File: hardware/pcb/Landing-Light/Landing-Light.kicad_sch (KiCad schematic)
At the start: 51 parts, among them J1 Conn_01x04, J3 USB_C_Receptacle_USB2.0_16P, Q2 NMOS, Q3 NMOS, Q4 PMOS, SW1 SW_SPDT, SW2 SW_SP3T, U1 BQ25172DSGR, U2 SRV05-4, U3 TPS61200DRC

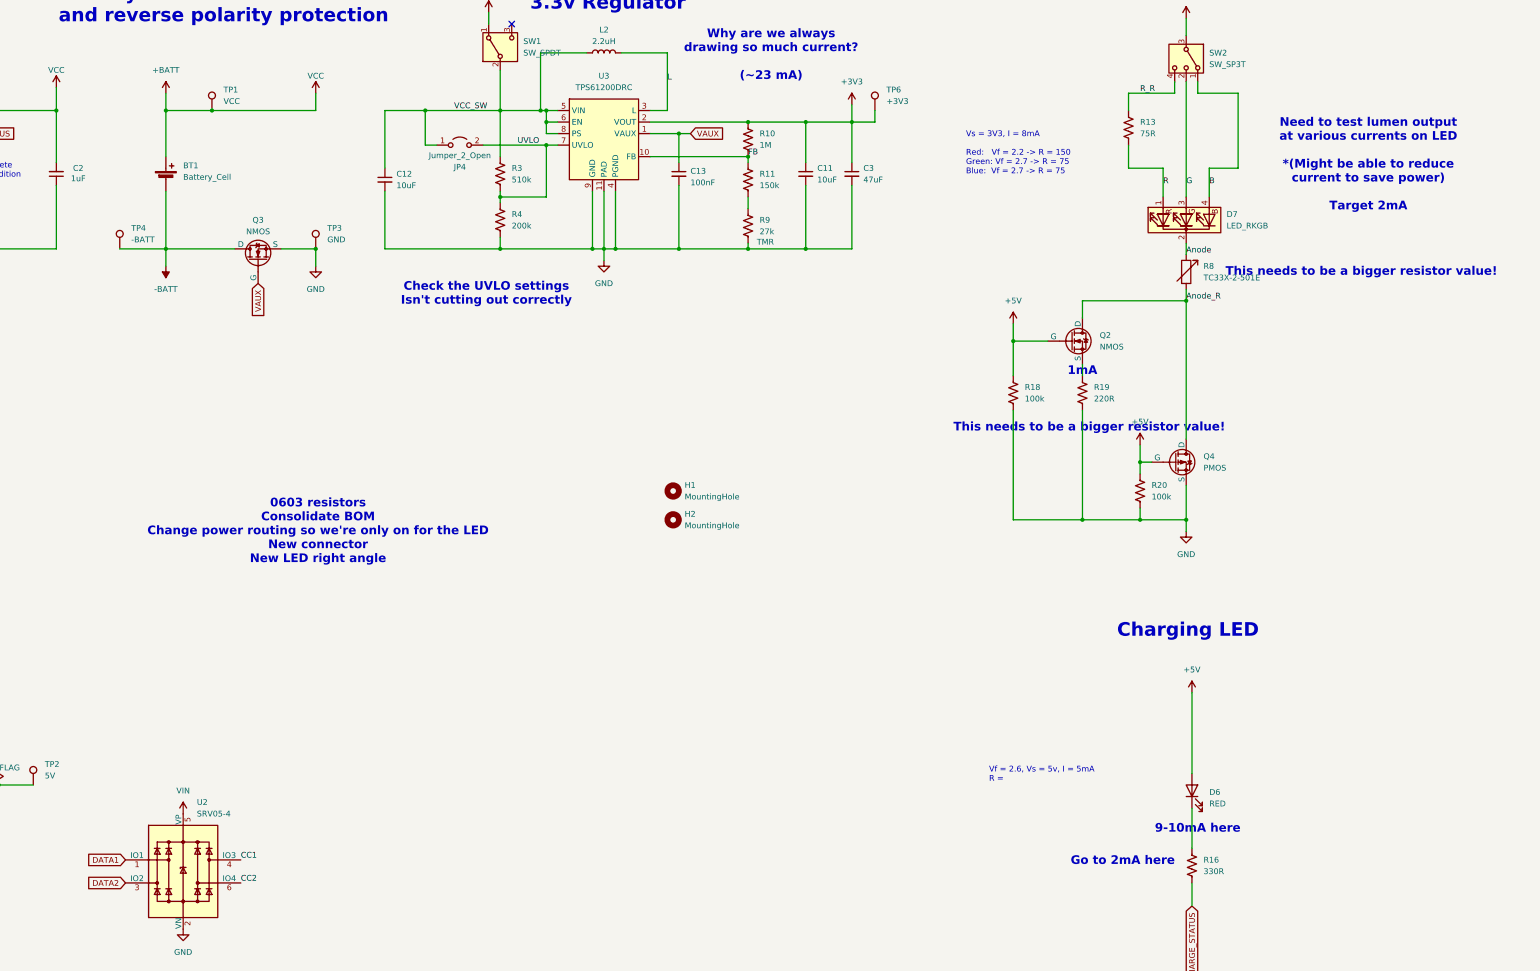
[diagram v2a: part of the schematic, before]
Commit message: Clean ground plane
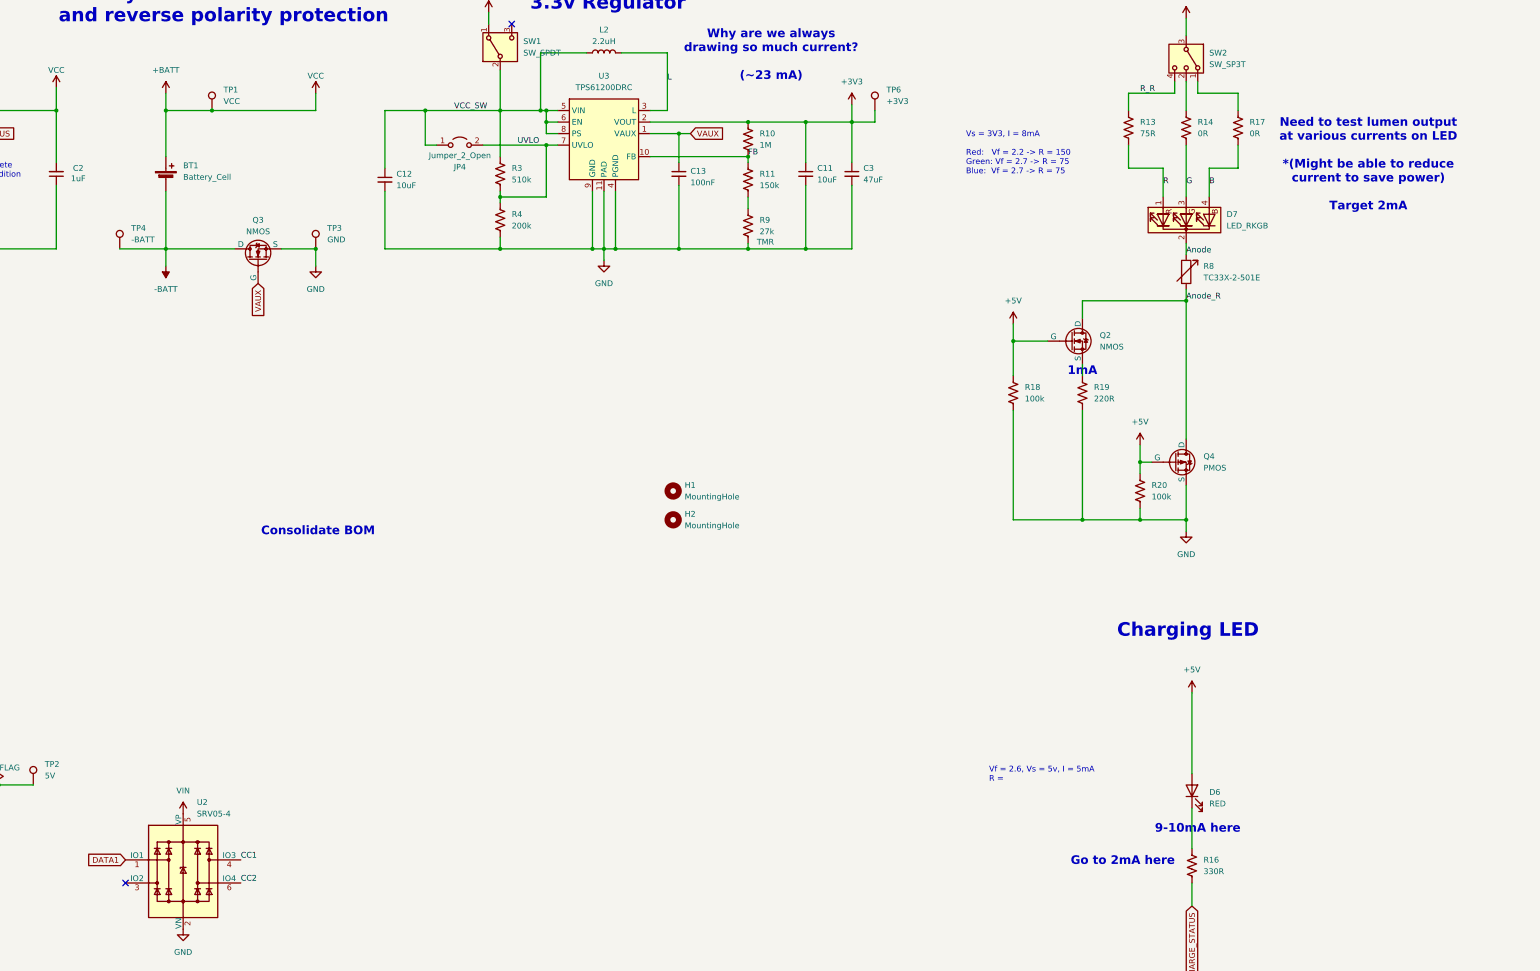
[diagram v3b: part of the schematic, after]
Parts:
- added R14, R17: 0R, Resistor_SMD:R_0402_1005Metric, symbol Device:R_US
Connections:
- net B: now also R17.2; no longer SW2.1
- net DATA2: no longer U2.3 (IO2)
- net G: now also R14.2; no longer SW2.2
- new net: R17.1, SW2.1
- new net: R14.1, SW2.2
- no-connect marks 7 -> 8
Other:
- note added: "Consolidate BOM"
- note removed: "0603 resistors Consolidate BOM Change power routing so we're only on for the LED New connector New LED right angle"
- note removed: "Check the UVLO settings Isn't cutting out correctly"
- note removed: "This needs to be a bigger resistor value!"
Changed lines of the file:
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@@
 	(generator_version "9.0")
 	(paper "A3")
-	(text "This needs to be a bigger resistor value!"
-		(exclude_from_sim no)
-		(at 418.338 88.9 0)
-		(effects
-			(font
-				(size 1.905 1.905)
-				(thickness 0.381)
-				(bold yes)
-				(color 255 0 0 1)
-			)
-		)
-	)
 	(text "Battery \nand reverse polarity protection"
 		(exclude_from_sim no)
@@
 		)
 	)
-	(text "This needs to be a bigger resistor value!"
-		(exclude_from_sim no)
-		(at 358.394 123.19 0)
-		(effects
-			(font
-				(size 1.905 1.905)
-				(thickness 0.381)
-				(bold yes)
-				(color 255 0 0 1)
-			)
-		)
-	)
-	(text "0603 resistors\nConsolidate BOM\nChange power routing so we're only on for the LED\nNew connector\nNew LED right angle"
+	(text "Consolidate BOM"
 		(exclude_from_sim no)
 		(at 188.468 146.05 0)
@@
 		)
 	)
-	(text "Check the UVLO settings\nIsn't cutting out correctly"
-		(exclude_from_sim no)
-		(at 225.552 93.726 0)
-		(effects
-			(font
-				(size 1.905 1.905)
-				(thickness 0.381)
-				(bold yes)
-				(color 255 0 0 1)
-			)
-		)
-	)
 	(text "USB-C Connector"
 		(exclude_from_sim no)
@@
 		(at 66.04 217.17)
 	)
+	(no_connect
+		(at 146.05 223.52)
+	)
 	(wire
 		(pts
@@
 	(wire
 		(pts
+			(xy 391.16 60.96) (xy 391.16 66.04)
+		)
+		(stroke
+			(width 0)
+			(type default)
+		)
+	)
+	(wire
+		(pts
 			(xy 356.87 109.22) (xy 356.87 111.76)
 		)
@@
 	(wire
 		(pts
+			(xy 391.16 49.53) (xy 391.16 53.34)
+		)
+		(stroke
+			(width 0)
+			(type default)
+		)
+	)
+	(wire
+		(pts
 			(xy 261.62 63.5) (xy 283.21 63.5)
 		)
@@
 	(wire
 		(pts
+			(xy 379.73 60.96) (xy 379.73 72.39)
+		)
+		(stroke
+			(width 0)
+			(type default)
+		)
+	)
+	(wire
+		(pts
 			(xy 379.73 143.51) (xy 379.73 146.05)
 		)
@@
 	(wire
 		(pts
-			(xy 379.73 46.99) (xy 379.73 72.39)
+			(xy 71.12 83.82) (xy 88.9 83.82)
 		)
 		(stroke
@@
 	(wire
 		(pts
-			(xy 71.12 83.82) (xy 88.9 83.82)
+			(xy 295.91 64.77) (xy 295.91 55.88)
 		)
 		(stroke
@@
 	(wire
 		(pts
-			(xy 295.91 64.77) (xy 295.91 55.88)
+			(xy 73.66 209.55) (xy 66.04 209.55)
 		)
 		(stroke
@@
 	(wire
 		(pts
-			(xy 73.66 209.55) (xy 66.04 209.55)
+			(xy 72.39 181.61) (xy 72.39 179.07)
 		)
 		(stroke
@@
 	(wire
 		(pts
-			(xy 72.39 181.61) (xy 72.39 179.07)
+			(xy 228.6 63.5) (xy 228.6 53.34)
 		)
 		(stroke
@@
 	(wire
 		(pts
-			(xy 228.6 63.5) (xy 228.6 53.34)
+			(xy 379.73 46.99) (xy 379.73 53.34)
 		)
 		(stroke
@@
 	(wire
 		(pts
-			(xy 391.16 49.53) (xy 391.16 66.04)
-		)
-		(stroke
-			(width 0)
-			(type default)
-		)
-	)
-	(wire
-		(pts
 			(xy 226.06 31.75) (xy 226.06 34.29)
 		)
@@
 		)
 	)
-	(global_label "DATA2"
-		(shape input)
-		(at 146.05 223.52 180)
-		(fields_autoplaced yes)
-		(effects
-			(font
-				(size 1.27 1.27)
-			)
-			(justify right)
-		)
-		(property "Intersheetrefs" "${INTERSHEET_REFS}"
-			(at 137.4405 223.52 0)
-			(effects
-				(font
-					(size 1.27 1.27)
-				)
-				(justify right)
-				(hide yes)
-			)
-		)
-	)
 	(global_label "DATA1"
 		(shape input)
-		(at 146.05 218.44 180)
+		(at 72.39 173.99 90)
 		(fields_autoplaced yes)
 		(effects
@@
 				(size 1.27 1.27)
 			)
-			(justify right)
+			(justify left)
 		)
 		(property "Intersheetrefs" "${INTERSHEET_REFS}"
-			(at 137.4405 218.44 0)
+			(at 72.39 165.3805 90)
 			(effects
 				(font
 					(size 1.27 1.27)
 				)
-				(justify right)
+				(justify left)
 				(hide yes)
 			)
 		)
 	)
-	(global_label "DATA1"
+	(global_label "VAUX"
 		(shape input)
-		(at 72.39 173.99 90)
+		(at 270.51 58.42 0)
 		(fields_autoplaced yes)
 		(effects
@@
 		)
 		(property "Intersheetrefs" "${INTERSHEET_REFS}"
-			(at 72.39 165.3805 90)
+			(at 278.2124 58.42 0)
 			(effects
 				(font
@@
 	(global_label "VAUX"
 		(shape input)
-		(at 270.51 58.42 0)
+		(at 175.26 91.44 270)
 		(fields_autoplaced yes)
 		(effects
@@
 				(size 1.27 1.27)
 			)
-			(justify left)
+			(justify right)
 		)
 		(property "Intersheetrefs" "${INTERSHEET_REFS}"
-			(at 278.2124 58.42 0)
+			(at 175.26 99.1424 90)
 			(effects
 				(font
 					(size 1.27 1.27)
 				)
-				(justify left)
+				(justify right)
 				(hide yes)
 			)
 		)
 	)
-	(global_label "VAUX"
+	(global_label "DATA1"
 		(shape input)
-		(at 175.26 91.44 270)
+		(at 146.05 218.44 180)
 		(fields_autoplaced yes)
 		(effects
@@
 		)
 		(property "Intersheetrefs" "${INTERSHEET_REFS}"
-			(at 175.26 99.1424 90)
+			(at 137.4405 218.44 0)
 			(effects
 				(font
@@
 	)
 	(symbol
+		(lib_id "Device:R_US")
+		(at 391.16 57.15 0)
+		(unit 1)
+		(exclude_from_sim no)
+		(in_bom yes)
+		(on_board yes)
+		(dnp no)
+		(property "Reference" "R17"
+			(at 393.7 55.8799 0)
+			(effects
+				(font
+					(size 1.27 1.27)
+				)
+				(justify left)
+			)
+		)
+		(property "Value" "0R"
+			(at 393.7 58.4199 0)
+			(effects
+				(font
+					(size 1.27 1.27)
+				)
+				(justify left)
+			)
+		)
+		(property "Footprint" "Resistor_SMD:R_0402_1005Metric"
+			(at 392.176 57.404 90)
+			(effects
+				(font
+					(size 1.27 1.27)
+				)
+				(hide yes)
+			)
+		)
+		(property "Datasheet" "~"
+			(at 391.16 57.15 0)
+			(effects
+				(font
+					(size 1.27 1.27)
+				)
+				(hide yes)
+			)
+		)
+		(property "Description" ""
+			(at 394.97 60.706 0)
+			(effects
+				(font
+					(size 1.27 1.27)
+				)
+			)
+		)
+		(property "LCSC" "C17168"
+			(at 391.16 57.15 0)
+			(effects
+				(font
+					(size 1.27 1.27)
+				)
+				(hide yes)
+			)
+		)
+		(pin "1"
+		)
+		(pin "2"
+		)
+		(instances
+			(project "Landing-Light"
+				(path "/f89d3217-1b1a-43a4-8c74-9ff6f0eaa6ee"
+					(reference "R17")
+					(unit 1)
+				)
+			)
+		)
+	)
+	(symbol
 		(lib_id "power:VDC")
 		(at 60.96 171.45 0)
@@
 					(unit 1)
 				)
+			)
+		)
+	)
+	(symbol
+		(lib_id "Device:R_US")
+		(at 379.73 57.15 0)
+		(unit 1)
+		(exclude_from_sim no)
+		(in_bom yes)
+		(on_board yes)
+		(dnp no)
+		(property "Reference" "R14"
+			(at 382.27 55.8799 0)
+			(effects
+				(font
+					(size 1.27 1.27)
+				)
+				(justify left)
+			)
+		)
+		(property "Value" "0R"
+			(at 382.27 58.4199 0)
+			(effects
+				(font
+					(size 1.27 1.27)
+				)
+				(justify left)
+			)
+		)
+		(property "Footprint" "Resistor_SMD:R_0402_1005Metric"
+			(at 380.746 57.404 90)
+			(effects
+				(font
+					(size 1.27 1.27)
+				)
+				(hide yes)
+			)
+		)
+		(property "Datasheet" "~"
+			(at 379.73 57.15 0)
+			(effects
+				(font
+					(size 1.27 1.27)
+				)
+				(hide yes)
+			)
+		)
+		(property "Description" ""
+			(at 383.54 60.706 0)
+			(effects
+				(font
+					(size 1.27 1.27)
+				)
+			)
+		)
+		(property "LCSC" "C17168"
+			(at 379.73 57.15 0)
+			(effects
+				(font
+					(size 1.27 1.27)
+				)
+				(hide yes)
+			)
+		)
+		(pin "1"
+		)
+		(pin "2"
+		)
+		(instances
+			(project "Landing-Light"
+				(path "/f89d3217-1b1a-43a4-8c74-9ff6f0eaa6ee"
+					(reference "R14")
+					(unit 1)
+				)

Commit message: Finalise BOM
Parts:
- J3: LCSC (none) -> C2894897
- R12, R15: footprint Resistor_SMD:R_0603_1608Metric -> Resistor_SMD:R_0402_1005Metric; LCSC C23186 -> C25905
- R16: value 330R -> 1.5k; LCSC C25104 -> C25867
- R18, R20: value 100k -> 150k; footprint Resistor_SMD:R_0603_1608Metric -> Resistor_SMD:R_0402_1005Metric; LCSC C25803 -> C25755
- R19: footprint Resistor_SMD:R_0603_1608Metric -> Resistor_SMD:R_0402_1005Metric
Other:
- note added: "1.6mA"
- note removed: "9-10mA here"
- note removed: "Go to 2mA here"
- moved on the sheet: Q2, Q4, R18, R19, R20

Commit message: v1.1 production
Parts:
- C3: now not fitted; now left out of the parts list
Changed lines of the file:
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@@
 		(unit 1)
 		(exclude_from_sim no)
-		(in_bom yes)
+		(in_bom no)
 		(on_board yes)
-		(dnp no)
+		(dnp yes)
 		(fields_autoplaced yes)
 		(property "Reference" "C3"

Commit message: Change charger connection point
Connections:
- net -BATT: now also C1.1, C2.1, R2.2, R5.2, R6.2, R7.2, U1.4 (GND), U1.9 (EXP)
- net GND: no longer C1.1, C2.1, R2.2, R5.2, R6.2, R7.2, U1.4 (GND), U1.9 (EXP)
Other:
- note added: "4.7kR here. Calculate current"
- note added: "BAttery charger needs to be connected to -BATT not GND"
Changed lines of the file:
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@@
 		)
 	)
+	(text "4.7kR here. Calculate current"
+		(exclude_from_sim no)
+		(at 418.084 88.646 0)
+		(effects
+			(font
+				(size 1.905 1.905)
+				(thickness 0.381)
+				(bold yes)
+				(color 255 0 0 1)
+			)
+		)
+	)
 	(text "Why are we always \ndrawing so much current?\n\n(~23 mA)"
 		(exclude_from_sim no)
@@
 		)
 	)
+	(text "BAttery charger needs to be connected to -BATT not GND"
+		(exclude_from_sim no)
+		(at 134.366 102.616 0)
+		(effects
+			(font
+				(size 1.905 1.905)
+				(thickness 0.381)
+				(bold yes)
+				(color 255 0 0 1)
+			)
+		)
+	)
 	(junction
 		(at 46.99 242.57)
@@
 	)
 	(junction
+		(at 144.78 83.82)
+		(diameter 0)
+		(color 0 0 0 0)
+	)
+	(junction
 		(at 228.6 53.34)
 		(diameter 0)
@@
 	)
 	(junction
-		(at 154.94 53.34)
+		(at 130.81 83.82)
 		(diameter 0)
 		(color 0 0 0 0)
 	)
 	(junction
-		(at 283.21 83.82)
+		(at 154.94 53.34)
 		(diameter 0)
 		(color 0 0 0 0)
 	)
 	(junction
-		(at 88.9 83.82)
+		(at 283.21 83.82)
 		(diameter 0)
 		(color 0 0 0 0)
@@
 	(wire
 		(pts
+			(xy 130.81 53.34) (xy 154.94 53.34)
+		)
+		(stroke
+			(width 0)
+			(type default)
+		)
+	)
+	(wire
+		(pts
 			(xy 261.62 63.5) (xy 283.21 63.5)
 		)
@@
 	(wire
 		(pts
+			(xy 130.81 83.82) (xy 144.78 83.82)
+		)
+		(stroke
+			(width 0)
+			(type default)
+		)
+	)
+	(wire
+		(pts
 			(xy 267.97 58.42) (xy 267.97 64.77)
 		)
@@
 	(wire
 		(pts
-			(xy 88.9 83.82) (xy 104.14 83.82)
+			(xy 71.12 83.82) (xy 104.14 83.82)
 		)
 		(stroke
@@
 	(wire
 		(pts
-			(xy 88.9 83.82) (xy 88.9 92.71)
-		)
-		(stroke
-			(width 0)
-			(type default)
-		)
-	)
-	(wire
-		(pts
-			(xy 71.12 83.82) (xy 88.9 83.82)
-		)
-		(stroke
-			(width 0)
-			(type default)
-		)
-	)
-	(wire
-		(pts
 			(xy 295.91 64.77) (xy 295.91 55.88)
 		)
@@
 	(wire
 		(pts
-			(xy 130.81 48.26) (xy 130.81 53.34)
-		)
-		(stroke
-			(width 0)
-			(type default)
-		)
-	)
-	(wire
-		(pts
 			(xy 90.17 224.79) (xy 90.17 241.3)
 		)
@@
 	)
 	(symbol
-		(lib_id "power:VCC")
-		(at 130.81 48.26 0)
-		(unit 1)
-		(exclude_from_sim no)
-		(in_bom yes)
-		(on_board yes)
-		(dnp no)
-		(fields_autoplaced yes)
-		(property "Reference" "#PWR026"
-			(at 130.81 52.07 0)
-			(effects
-				(font
-					(size 1.27 1.27)
-				)
-				(hide yes)
-			)
-		)
-		(property "Value" "VCC"
-			(at 130.81 44.45 0)
-			(effects
-				(font
-					(size 1.27 1.27)
-				)
-			)
-		)
-		(property "Footprint" ""
-			(at 130.81 48.26 0)
-			(effects
-				(font
-					(size 1.27 1.27)
-				)
-				(hide yes)
-			)
-		)
-		(property "Datasheet" ""
-			(at 130.81 48.26 0)
-			(effects
-				(font
-					(size 1.27 1.27)
-				)
-				(hide yes)
-			)
-		)
-		(property "Description" ""
-			(at 130.81 48.26 0)
-			(effects
-				(font
-					(size 1.27 1.27)
-				)
-				(hide yes)
-			)
-		)
-		(pin "1"
-		)
-		(instances
-			(project "Landing-Light"
-				(path "/f89d3217-1b1a-43a4-8c74-9ff6f0eaa6ee"
-					(reference "#PWR026")
-					(unit 1)
-				)
-			)
-		)
-	)
-	(symbol
 		(lib_id "power:PWR_FLAG")
 		(at 118.11 201.93 0)
@@
 					(unit 1)
 				)
-			)
-		)
-	)
-	(symbol
-		(lib_id "power:GND")
-		(at 88.9 92.71 0)
-		(unit 1)
-		(exclude_from_sim no)
-		(in_bom yes)
-		(on_board yes)
-		(dnp no)
-		(fields_autoplaced yes)
-		(property "Reference" "#PWR03"
-			(at 88.9 99.06 0)
-			(effects
-				(font
-					(size 1.27 1.27)
-				)
-				(hide yes)
-			)
-		)
-		(property "Value" "GND"
-			(at 88.9 97.79 0)
-			(effects
-				(font
-					(size 1.27 1.27)
-				)
-			)
-		)
-		(property "Footprint" ""
-			(at 88.9 92.71 0)
-			(effects
-				(font
-					(size 1.27 1.27)
-				)
-				(hide yes)
-			)
-		)
-		(property "Datasheet" ""
-			(at 88.9 92.71 0)
-			(effects
-				(font
-					(size 1.27 1.27)
-				)
-				(hide yes)
-			)
-		)
-		(property "Description" "Power symbol creates a global label with name \"GND\" , ground"
-			(at 88.9 92.71 0)
-			(effects
-				(font
-					(size 1.27 1.27)
-				)
-				(hide yes)
-			)
-		)
-		(pin "1"
-		)
-		(instances
-			(project "Landing-Light"
-				(path "/f89d3217-1b1a-43a4-8c74-9ff6f0eaa6ee"
-					(reference "#PWR03")
-					(unit 1)
-				)

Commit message: v1.2 notes and structure
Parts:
- removed C3: 47uF, Capacitor_SMD:C_0603_1608Metric, symbol Device:C_Small
- removed R8: TC33X-2-501E, Potentiometer_SMD:Potentiometer_Bourns_TC33X_Vertical, symbol Device:R_Variable
- added JP1: SolderJumper_3_Bridged12, Jumper:SolderJumper-3_P1.3mm_Bridged2Bar12_RoundedPad1.0x1.5mm, symbol Jumper:SolderJumper_3_Bridged12
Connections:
- net GND: now also JP1.1 (A)
- net VCC_SW: now also JP1.3 (B); no longer U3.8 (PS)
- new net: JP1.2 (C), U3.8 (PS)
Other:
- note added: "Consider switching to 680k 220k to raise UVLO to 1.025V from 0.89V"
- note added: "It's the jumper - pull PS low"
- note added: "Todo: Fix battery charging when "off" Replace LED variable resistor with two options for brightness Recalculate UVLO resistors for 1.0V cutoff Add side mount LED Consolidate BOM Increment revision number"
- note removed: "BAttery charger needs to be connected to -BATT not GND"
- note removed: "Why are we always drawing so much current? (~23 mA)"
- moved on the sheet: C12

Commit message: Restructuring power flow for clarity
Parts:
- removed JP4: Jumper_2_Open, Jumper:SolderJumper-2_P1.3mm_Open_RoundedPad1.0x1.5mm, symbol Jumper:Jumper_2_Open
- removed R13: 75R, Resistor_SMD:R_0402_1005Metric, symbol Device:R_US
- removed R14, R17: 0R, Resistor_SMD:R_0402_1005Metric, symbol Device:R_US
- added JP2: LED Bridge, symbol Jumper:SolderJumper_3_Bridged12
- added R1: 5.6k, Resistor_SMD:R_0402_1005Metric, symbol Device:R_US
- added R8: 1.5k, Resistor_SMD:R_0402_1005Metric, symbol Device:R_US
- JP1: value SolderJumper_3_Bridged12 -> PS Bridge
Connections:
- net R_R is gone; now on net R: SW2.4
- net -BATT: now also C10.2, C8.2, C9.1, R12.2, R15.2
- net Anode: now also R1.1, R8.1
- net Anode_R: now also JP2.2 (C)
- net B: now also SW2.1
- net G: now also SW2.2
- net GND: no longer C10.2, C8.2, C9.1, R12.2, R15.2
- net PS: now reaches JP1.2 (C), U3.8 (PS)
- new net: JP2.1 (A), R1.2
- new net: JP2.3 (B), R8.2
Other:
- note removed: "It's the jumper - pull PS low"
- note removed: "Need to test lumen output at various currents on LED *(Might be able to reduce current to save power) Target 2mA"
- moved on the sheet: BT1, C1, C10, C11, C12, C13, C2, C8, C9, D6, D7, FB1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
